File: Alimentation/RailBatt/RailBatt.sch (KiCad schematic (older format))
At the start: 8 parts, among them J1 Batt1, J2 Batt3, J3 Batt5, J4 Batt4, J5 Batt2, J6 Batt6

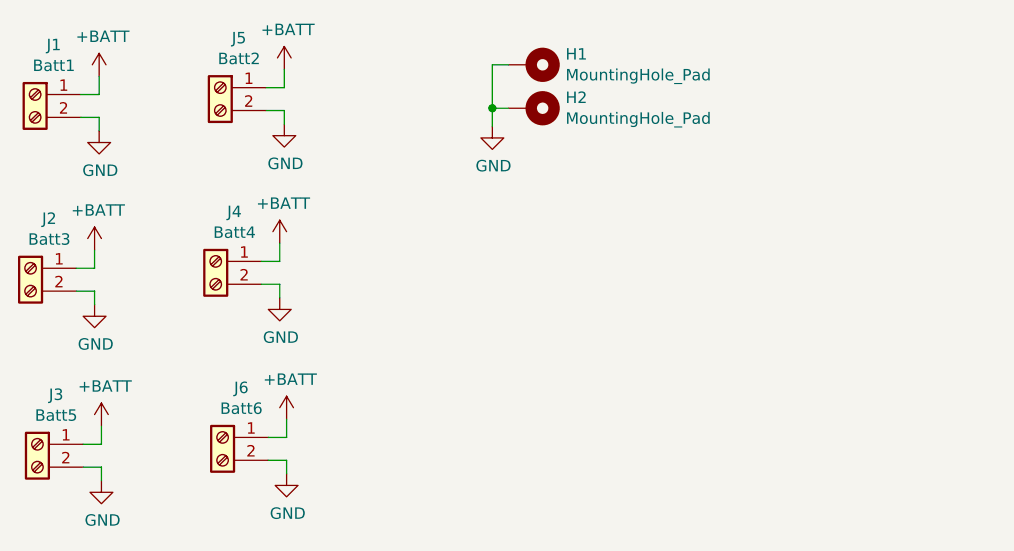
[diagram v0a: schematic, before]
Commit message: Réduction de taille rail alimentation (fusion borniers)
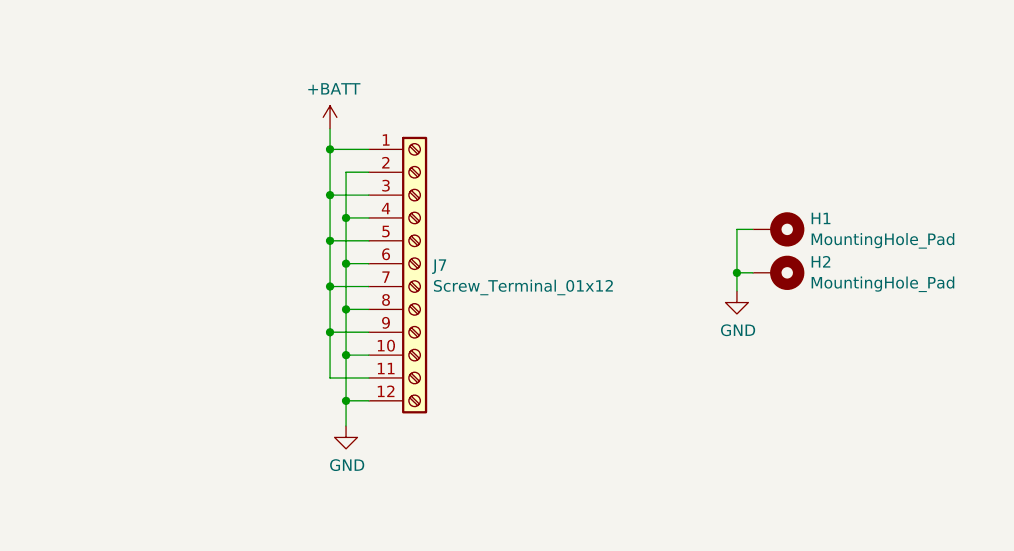
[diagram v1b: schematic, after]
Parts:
- removed J1: Batt1, TerminalBlock_Phoenix:TerminalBlock_Phoenix_MKDS-1,5-2-5.08_1x02_P5.08mm_Horizontal, symbol Connector:Screw_Terminal_01x02
- removed J2: Batt3, TerminalBlock_Phoenix:TerminalBlock_Phoenix_MKDS-1,5-2-5.08_1x02_P5.08mm_Horizontal, symbol Connector:Screw_Terminal_01x02
- removed J3: Batt5, TerminalBlock_Phoenix:TerminalBlock_Phoenix_MKDS-1,5-2-5.08_1x02_P5.08mm_Horizontal, symbol Connector:Screw_Terminal_01x02
- removed J4: Batt4, TerminalBlock_Phoenix:TerminalBlock_Phoenix_MKDS-1,5-2-5.08_1x02_P5.08mm_Horizontal, symbol Connector:Screw_Terminal_01x02
- removed J5: Batt2, TerminalBlock_Phoenix:TerminalBlock_Phoenix_MKDS-1,5-2-5.08_1x02_P5.08mm_Horizontal, symbol Connector:Screw_Terminal_01x02
- removed J6: Batt6, TerminalBlock_Phoenix:TerminalBlock_Phoenix_MKDS-1,5-2-5.08_1x02_P5.08mm_Horizontal, symbol Connector:Screw_Terminal_01x02
- added J7: Screw_Terminal_01x12, TerminalBlock_Phoenix:TerminalBlock_Phoenix_MKDS-1,5-12-5.08_1x12_P5.08mm_Horizontal, symbol Connector:Screw_Terminal_01x12
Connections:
- net +BATT: now also J7.1 (Pin_1), J7.11 (Pin_11), J7.3 (Pin_3), J7.5 (Pin_5), J7.7 (Pin_7), J7.9 (Pin_9)
- net GND: now also J7.10 (Pin_10), J7.12 (Pin_12), J7.2 (Pin_2), J7.4 (Pin_4), J7.6 (Pin_6), J7.8 (Pin_8)
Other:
- moved on the sheet: H1, H2
